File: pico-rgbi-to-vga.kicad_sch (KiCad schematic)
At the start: 25 parts, among them J1 SDS-80J, J2 DB15_Female_HighDensity, J3 USB-B1HSB6, SW1 SW_Push, SW2 Intensity Select, U1 Pico

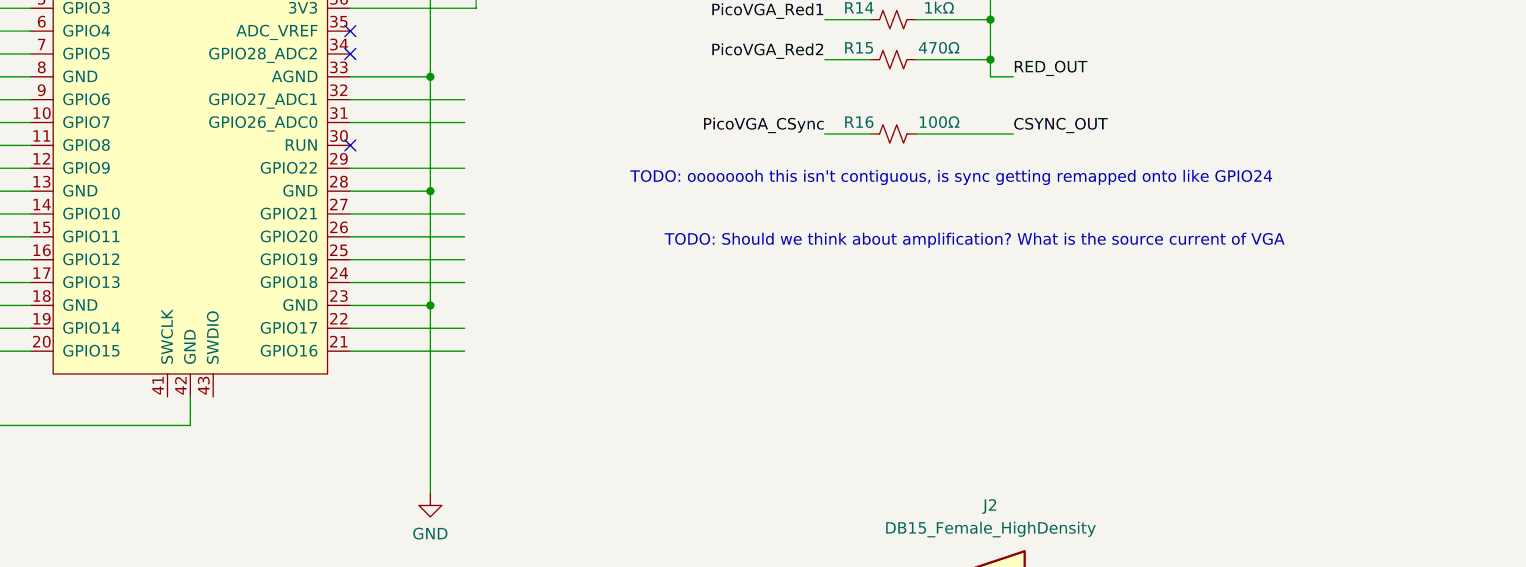
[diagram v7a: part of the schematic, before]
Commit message: V0.3 prep, adding logic analyzer lines
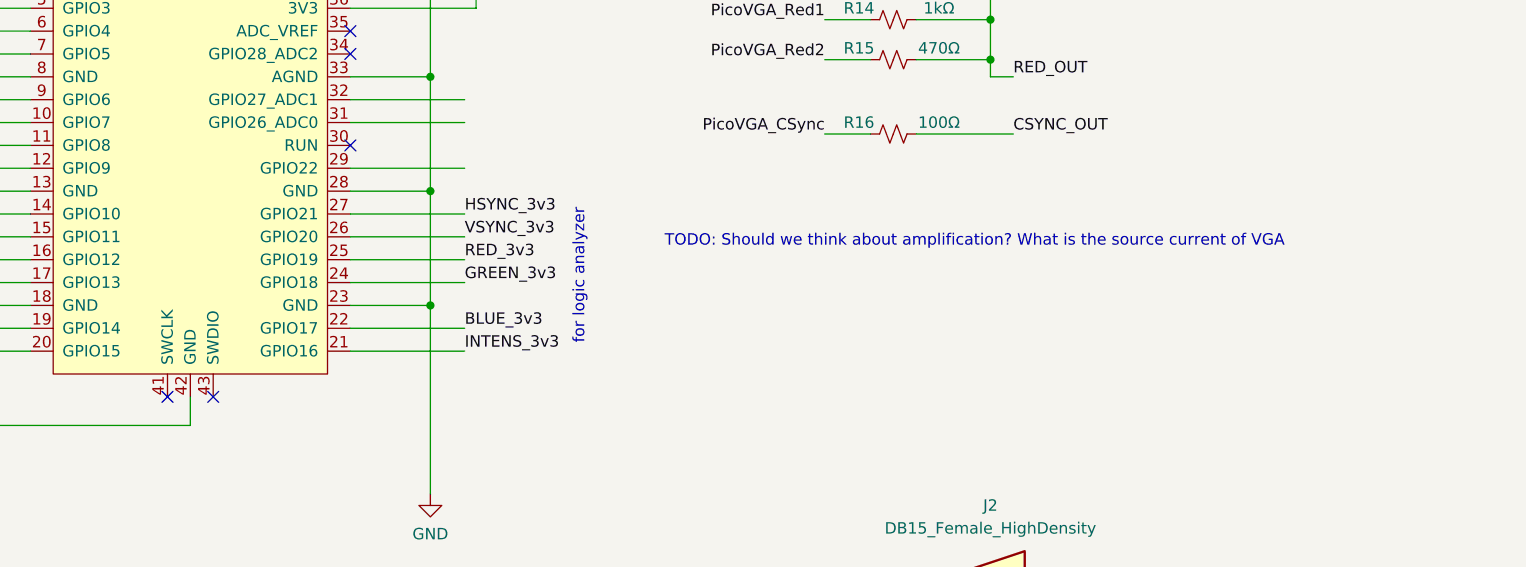
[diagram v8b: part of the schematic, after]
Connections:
- net BLUE_3v3: now also U1.22 (GPIO17)
- net GREEN_3v3: now also U1.24 (GPIO18)
- net HSYNC_3v3: now also U1.27 (GPIO21)
- net INTENS_3v3: now also U1.21 (GPIO16)
- net RED_3v3: now also U1.25 (GPIO19)
- net VSYNC_3v3: now also U1.26 (GPIO20)
- no-connect marks 13 -> 15
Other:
- note added: "for logic analyzer"
- note removed: "TODO: oooooooh this isn't contiguous, is sync getting remapped onto like GPIO24"
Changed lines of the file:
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@@
+	)
+	(no_connect
+		(at 151.13 100.33)
 	)
 	(no_connect
@@
 	(no_connect
 		(at 234.95 137.795)
+	)
+	(no_connect
+		(at 156.21 100.33)
 	)
 	(no_connect
@@
 		)
 	)
-	(text "TODO: oooooooh this isn't contiguous, is sync getting remapped onto like GPIO24"
+	(text "for logic analyzer"
 		(exclude_from_sim no)
-		(at 202.565 76.835 0)
-		(effects
-			(font
-				(size 1.27 1.27)
-			)
-			(justify left bottom)
+		(at 196.85 86.995 90)
+		(effects
+			(font
+				(size 1.27 1.27)
+			)
 		)
 	)
@@
 		)
 	)
+	(label "INTENS_3v3"
+		(at 184.15 95.25 0)
+		(fields_autoplaced yes)
+		(effects
+			(font
+				(size 1.27 1.27)
+			)
+			(justify left bottom)
+		)
+	)
 	(label "HSYNC_IN"
 		(at 54.61 97.155 180)
@@
 		)
 	)
+	(label "RED_3v3"
+		(at 184.15 85.09 0)
+		(fields_autoplaced yes)
+		(effects
+			(font
+				(size 1.27 1.27)
+			)
+			(justify left bottom)
+		)
+	)
+	(label "BLUE_3v3"
+		(at 184.15 92.71 0)
+		(fields_autoplaced yes)
+		(effects
+			(font
+				(size 1.27 1.27)
+			)
+			(justify left bottom)
+		)
+	)
+	(label "VSYNC_3v3"
+		(at 184.15 82.55 0)
+		(fields_autoplaced yes)
+		(effects
+			(font
+				(size 1.27 1.27)
+			)
+			(justify left bottom)
+		)
+	)
 	(label "HSYNC_3v3"
 		(at 131.445 62.23 180)
@@
 		)
 	)
+	(label "HSYNC_3v3"
+		(at 184.15 80.01 0)
+		(fields_autoplaced yes)
+		(effects
+			(font
+				(size 1.27 1.27)
+			)
+			(justify left bottom)
+		)
+	)
 	(label "RED_IN"
 		(at 53.34 135.89 180)
@@
 		)
 	)
+	(label "GREEN_3v3"
+		(at 184.15 87.63 0)
+		(fields_autoplaced yes)
+		(effects
+			(font
+				(size 1.27 1.27)
+			)
+			(justify left bottom)
+		)
+	)
